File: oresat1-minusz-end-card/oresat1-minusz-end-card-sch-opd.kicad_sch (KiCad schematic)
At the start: 51 parts, among them Q1 DMP2240UDM, Q2 PMV45EN, Q3 PMV45EN, Q4 PMV45EN, Q5 DMP2240UDM-7, Q6 PMV45EN, Q7 DMP2240UDM-7, U11 MIC842LYC5, U12 MIC842LYC5, U2 MAX7310

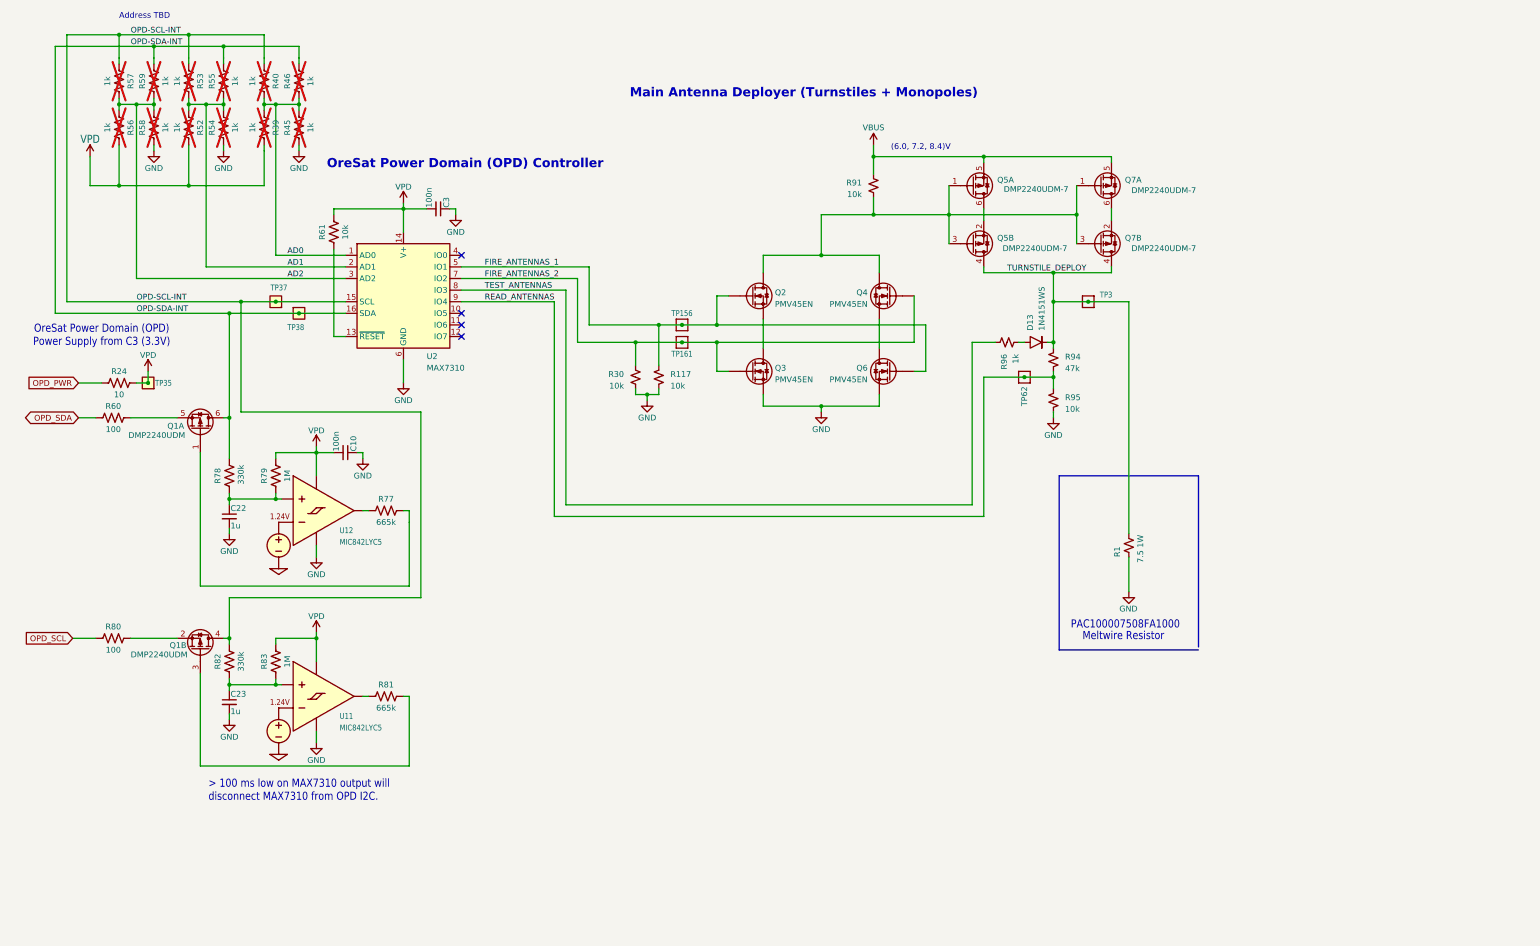
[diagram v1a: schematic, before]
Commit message: OreSat1 -Z end card update
Upgraded symbols, fixed BOM and added presets, and added UART switches for new solar modules. Clleaned up layout, including some planes and footprints. Still more left to do, but it's more ready to go.
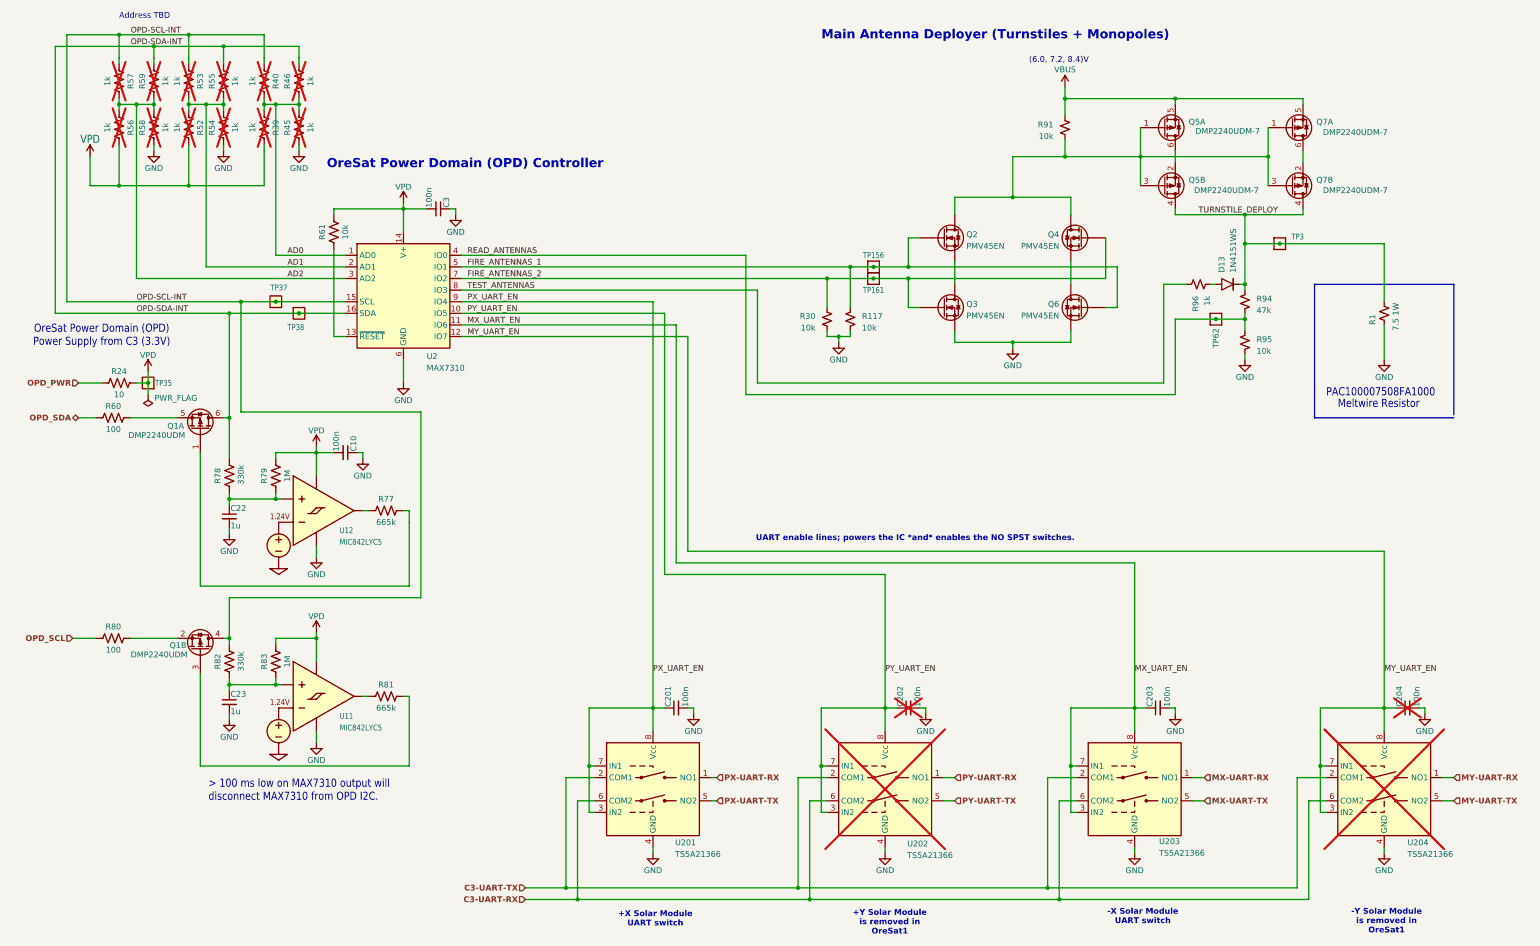
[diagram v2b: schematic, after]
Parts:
- added C201, C202, C203, C204: 100n, oresat-passives:0603-C-NOSILK, symbol Device:C_Small
- added U201, U202, U203, U204: TS5A21366, Package_SO:VSSOP-8_2.3x2mm_P0.5mm, symbol oresat-ics:TS5A21366
- D13: DIS (none) -> DigiKey; DST Digi-Key -> (none)
- R1: DIS (none) -> DigiKey; DPN (none) -> 749-PAC100007508FA1000CT-ND; MFR (none) -> Vishay; MPN (none) -> PAC100007508FA1000
- R117, R30, R91, R94, R95: footprint Resistor_SMD:R_0603_1608Metric -> oresat-passives:0603-C-NOSILK; DIS (none) -> DigiKey; DST Digi-Key -> (none); MFR Stackpole Electronics Inc -> Stackpole Electronics
- R24, R60, R61, R77, R78, R79, R80, R81, R82, R83: MFR Stackpole Electronics Inc -> Stackpole Electronics
- R39, R45, R46, R52, R53, R55, R56, R57, R59: DIS Digi-Key -> DigiKey; DPN 1276-4275-1-ND -> RMCF0603FT2K70CT-ND; MFR Samsung -> Stackpole Electronics; MPN RC1005F6653CS -> RMCF0603FT1K00
- R40, R54, R58: DPN RMCF0603FT1K00CT-ND -> RMCF0603FT2K70CT-ND; MFR Stackpole Electronics Inc -> Stackpole Electronics
- R96: footprint Resistor_SMD:R_0603_1608Metric -> oresat-passives:0603-C-NOSILK; DIS (none) -> DigiKey; DPN RMCF0603FT1K00CT-ND -> RMCF0603FT2K70CT-ND; DST Digi-Key -> (none); MFR Stackpole Electronics Inc -> Stackpole Electronics
- U2: MFR Maxim -> Analog Devices; MPN MAX7310ATE -> MAX7310ATE+
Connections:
- net GND: now also C201.2, C202.2, C203.2, C204.2, U201.4 (GND), U202.4 (GND), U203.4 (GND), U204.4 (GND)
- net READ_ANTENNAS: now also U2.4 (IO0); no longer U2.9 (IO4)
- net PY_UART_EN: now reaches U2.10 (IO5)
- net PY_UART_EN: now also C202.1, U202.3 (IN2), U202.7 (IN1), U202.8 (Vcc)
- net MX_UART_EN: now reaches U2.11 (IO6)
- net MX_UART_EN: now also C203.1, U203.3 (IN2), U203.7 (IN1), U203.8 (Vcc)
- net MY_UART_EN: now reaches U2.12 (IO7)
- net MY_UART_EN: now also C204.1, U204.3 (IN2), U204.7 (IN1), U204.8 (Vcc)
- new net C3-UART-RX: U201.6 (COM2), U202.6 (COM2), U203.6 (COM2), U204.6 (COM2)
- new net C3-UART-TX: U201.2 (COM1), U202.2 (COM1), U203.2 (COM1), U204.2 (COM1)
- new net MX-UART-RX: U203.1 (NO1)
- new net MX-UART-TX: U203.5 (NO2)
- new net MY-UART-RX: U204.1 (NO1)
- new net MY-UART-TX: U204.5 (NO2)
- new net PX-UART-RX: U201.1 (NO1)
- new net PX-UART-TX: U201.5 (NO2)
- new net PX_UART_EN: C201.1, U2.9 (IO4), U201.3 (IN2), U201.7 (IN1), U201.8 (Vcc)
- new net PY-UART-RX: U202.1 (NO1)
- new net PY-UART-TX: U202.5 (NO2)
- no-connect marks 4 -> 0
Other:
- note added: "+X Solar Module UART switch"
- note added: "+Y Solar Module is removed in OreSat1"
- note added: "-X Solar Module UART switch"
- note added: "-Y Solar Module is removed in OreSat1"
- note added: "UART enable lines; powers the IC *and* enables the NO SPST switches."
- moved on the sheet: D13, Q2, Q3, Q4, Q5A, Q5B, Q6, Q7A, Q7B, R1, R117, R30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
